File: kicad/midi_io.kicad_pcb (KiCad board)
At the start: 2 copper layers, 38.1 x 41.4 mm, 10 parts, among them J1 MIDI Out, J2 MIDI In, J3 Conn_01x04, U1 6N138

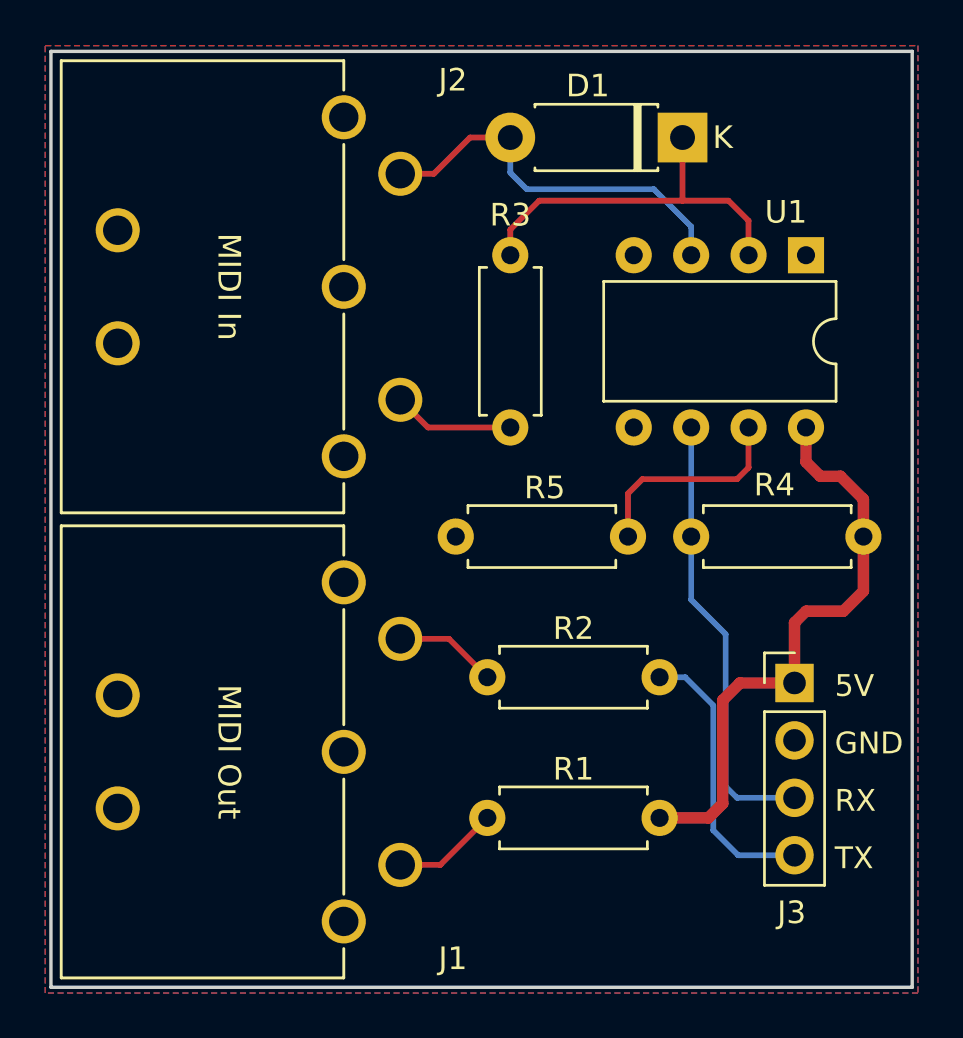
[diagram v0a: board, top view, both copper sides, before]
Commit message: Change to 0804 SMD resistors
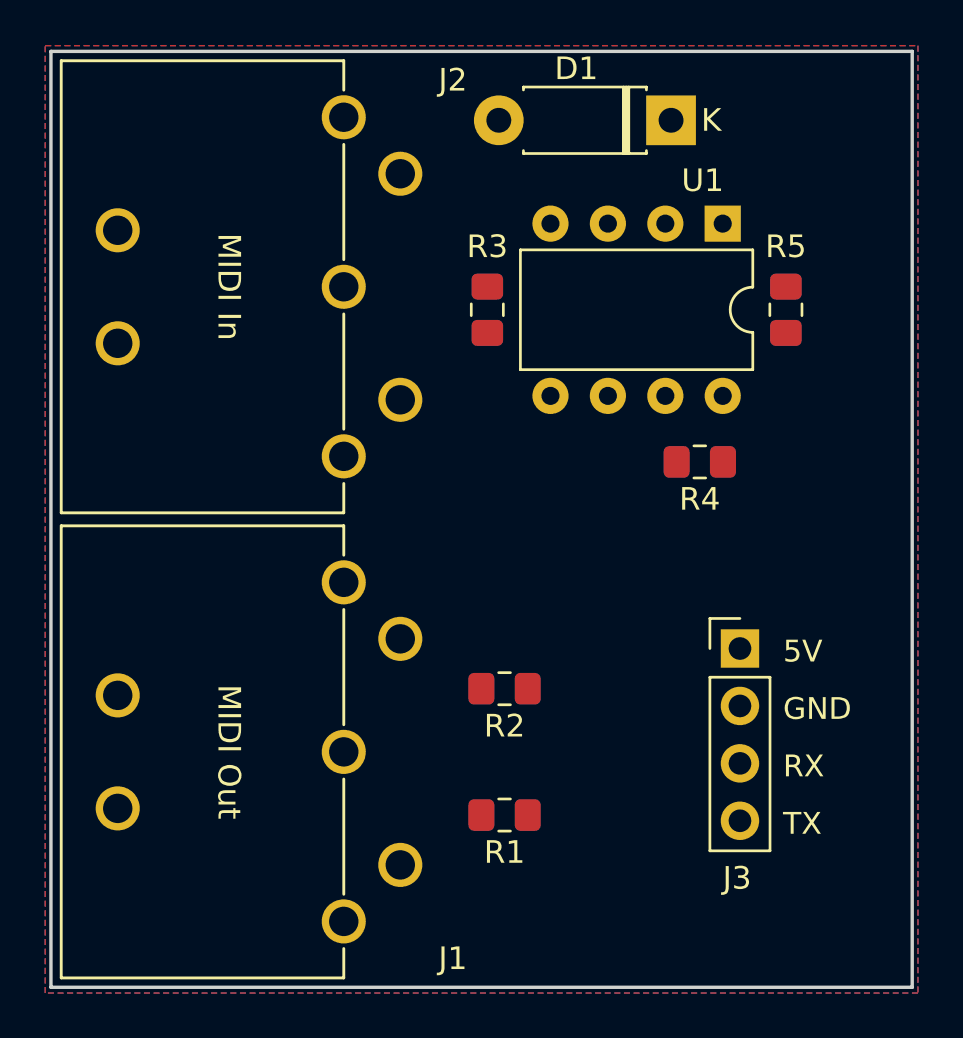
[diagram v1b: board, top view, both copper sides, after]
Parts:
- R1, R2, R3, R4, R5: footprint Resistor_THT:R_Axial_DIN0207_L6.3mm_D2.5mm_P7.62mm_Horizontal -> Resistor_SMD:R_0805_2012Metric_Pad1.15x1.40mm_HandSolder
- moved R5 12.2 mm to (143.5, 95.9), turned to 90 degrees
- moved R4 7.96 mm to (139.7, 102.6)
- moved R2 6.88 mm to (131.1, 112.6)
- moved R1 6.86 mm to (131.1, 118.2)
- moved U1 3.94 mm to (140.7, 92.1)
- moved J3 2.85 mm to (141.5, 110.9)
- moved R3 2.62 mm to (130.3, 95.9)
- moved D1 0.92 mm to (138.4, 87.5)
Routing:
- net VCC: track 26.2 -> 0.00 mm
- net /RX: track 19.8 -> 0.00 mm
- net Net-(D1-Pad2): track 17.3 -> 0.00 mm
- net Net-(D1-Pad1): track 16.9 -> 0.00 mm
- net /TX: track 12.5 -> 0.00 mm
- net Net-(R5-Pad1): track 9.49 -> 0.00 mm
- net Net-(J2-Pad4): track 5.37 -> 0.00 mm
- net Net-(J1-Pad4): track 4.71 -> 0.00 mm
- net Net-(J1-Pad5): track 4.55 -> 0.00 mm

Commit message: Re-route PCB
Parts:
- moved R5 13.2 mm to (131.1, 100.2), turned to 270 degrees
- moved R4 3.27 mm to (140.5, 105.8)
- moved U1 3.06 mm to (143.0, 94.1)
- moved J3 2.65 mm to (144.0, 111.6)
- moved R1 2.30 mm to (131.3, 120.5)
- moved R2 2.30 mm to (131.3, 110.4)
- moved D1 1.05 mm to (138.7, 88.5)
- moved R3 0.76 mm to (131.1, 95.9)
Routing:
- net VCC: track 0.00 -> 28.7 mm, vias 0 -> 2
- net /RX: track 0.00 -> 19.6 mm
- net /TX: track 0.00 -> 18.5 mm
- net Net-(D1-Pad1): track 0.00 -> 17.1 mm
- net Net-(D1-Pad2): track 0.00 -> 16.1 mm
- net Net-(R5-Pad1): track 0.00 -> 11.3 mm
- net Net-(J2-Pad4): track 0.00 -> 6.97 mm
- net Net-(J1-Pad5): track 0.00 -> 3.87 mm
- net Net-(J1-Pad4): track 0.00 -> 3.87 mm
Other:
- board size 38.1 x 41.4 mm -> 35.6 x 41.4 mm
